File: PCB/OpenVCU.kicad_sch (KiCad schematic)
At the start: 25 parts, among them U1 STM32H743VIT6, Y1 ABM8-272-T3, Y2 CM315D32768DZFT

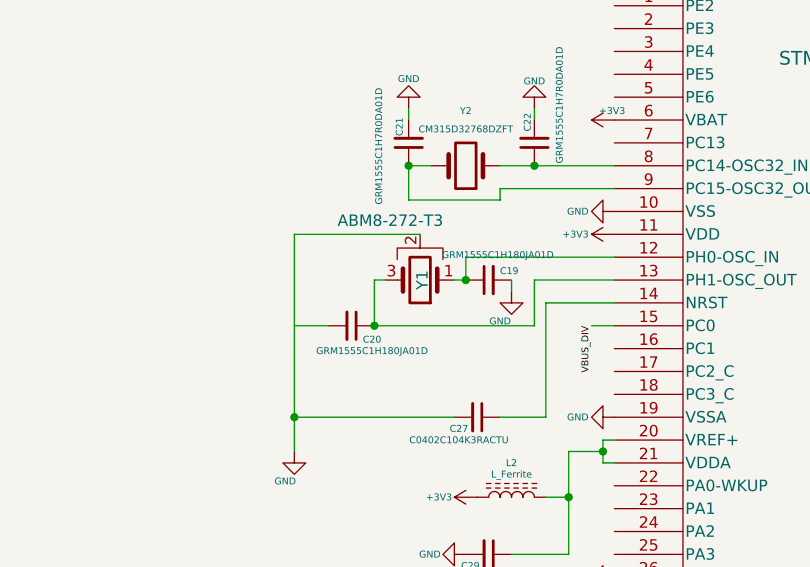
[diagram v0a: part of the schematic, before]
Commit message: Power sheet P2: USB-C fix, buck replacement, LDO rewire, battery sense, pull-downs
- Replaced MP1584 buck with TPS54360 (EOL fix)
- Fixed USB-C: CC pull-downs, ESD wiring, VBUS path, shell ground
- Rewired LDO: VIN<-+5V, GND->GND, VOUT->+3V3, caps at pins
- Added battery sense divider (100k/10k from VBAT)
- Added SBU1/SBU2 1M pull-downs (R38, R39)
- Fixed component rotations for distinct pin tips (90°)
- Added PWR_FLAGS on +5V rail (source) and VBUS net
- Added SBU1/SBU2 1M pull-downs (R38, R39)
- Removed old MP1584 debris
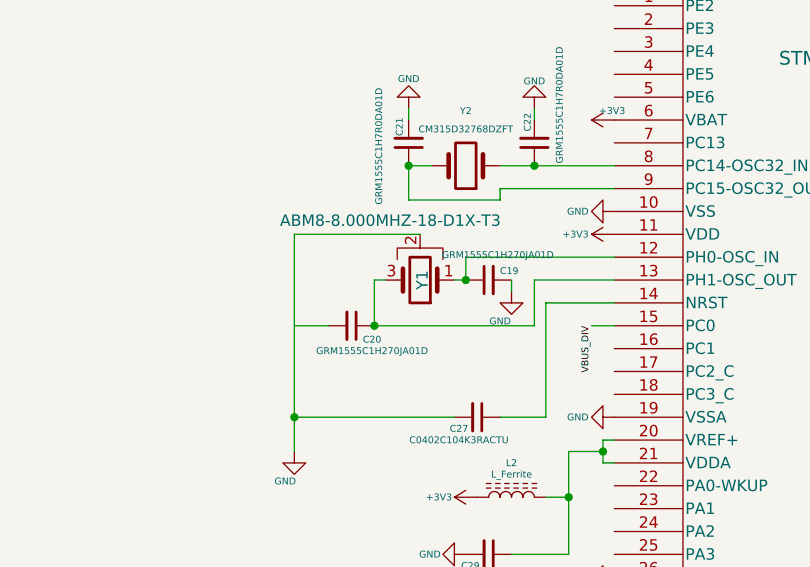
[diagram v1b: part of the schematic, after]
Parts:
- C19, C20: value GRM1555C1H180JA01D -> GRM1555C1H270JA01D; footprint GRM1555C1H180JA01D:CAPC1005X55N -> GRM1555C1H270JA01D:CAPC1005X55N; Check_prices https://www.snapeda.com/parts/GRM1555C1H180JA01D/Murata/vie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 -> https://www.snapeda.com/parts/GRM1555C1H270JA01D/Murata/vie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; MP GRM1555C1H180JA01D -> GRM1555C1H270JA01D; SnapEDA_Link https://www.snapeda.com/parts/GRM1555C1H180JA01D/Murata/vie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 -> https://www.snapeda.com/parts/GRM1555C1H270JA01D/Murata/vie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
- Y1: value ABM8-272-T3 -> ABM8-8.000MHZ-18-D1X-T3; footprint ABM8-272-T3:XTAL_ABM8-272-T3 -> ABM8-8.000MHZ-18-D1X-T3:XTAL_ABM8-8.000MHZ-18-D1X-T3; Check_prices https://www.snapeda.com/parts/ABM8-272-T3/Abracon/view-part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 -> https://www.snapeda.com/parts/ABM8-8.000MHZ-18-D1X-T3/Abrac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; MP ABM8-272-T3 -> ABM8-8.000MHZ-18-D1X-T3; Purchase-URL https://www.snapeda.com/api/url_track_click_mouser/?unipart_id=15805472&manufacturer=ABRACON&part_name=ABM8-272-T3&search_term=None -> https://www.snapeda.com/api/url_track_click_mouser/?unipart_id=15805472&manufacturer=ABRACON&part_name=ABM8-8.000MHZ-18-D1X-T3&search_term=None; SnapEDA_Link https://www.snapeda.com/parts/ABM8-272-T3/Abracon/view-part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 -> https://www.snapeda.com/parts/ABM8-8.000MHZ-18-D1X-T3/Abrac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

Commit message: Hierarchy: Power sheet hierarchical labels + root sheet pins (via Konnect)
- Added 5 hierarchical labels to Power.kicad_sch (VBAT, USB_D_P, USB_D_N, VBUS_SENSE, VBUS_DIV)
- Imported matching sheet pins onto root Power instance
- validate_sheet_pins: 0 issues; both files parse cleanly
- Root cause of A1: sub-sheets had only local labels, zero hierarchical labels
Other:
- sheet Power ports: added USB_D_N, USB_D_P, VBAT, VBUS_DIV, VBUS_SENSE; removed none
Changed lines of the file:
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@@
 			)
+		)
+		(pin "USB_D_P" bidirectional
+			(at 266.7 73.66 0)
+		)
+		(pin "USB_D_N" bidirectional
+			(at 266.7 76.2 0)
+		)
+		(pin "VBUS_SENSE" output
+			(at 266.7 78.74 0)
+		)
+		(pin "VBUS_DIV" output
+			(at 266.7 81.28 0)
+		)
+		(pin "VBAT" input
+			(at 266.7 83.82 0)
 		)
 		(instances

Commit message: Hierarchy: Sensors sheet hierarchical labels + root sheet pins (via Konnect)
- Added 8 hierarchical labels to Sensors.kicad_sch
- Fixed net-name mismatch: IMU_CS->SPI_CS_ACCEL, IMU_INT1->BMI_INT1 (match root MCU labels)
- Imported matching sheet pins on root Sensors instance
- validate_sheet_pins: 0 issues
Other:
- sheet Sensors ports: added BARO_INT, BMI_INT1, I2C1_SCL, I2C1_SDA, SPI1_MISO, SPI1_MOSI, SPI1_SCK, SPI_CS_ACCEL; removed none
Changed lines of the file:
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@@
 			)
+		)
+		(pin "SPI_CS_ACCEL" bidirectional
+			(at 266.7 38.1 0)
+		)
+		(pin "BMI_INT1" bidirectional
+			(at 266.7 40.64 0)
+		)
+		(pin "SPI1_SCK" bidirectional
+			(at 266.7 43.18 0)
+		)
+		(pin "SPI1_MOSI" bidirectional
+			(at 266.7 45.72 0)
+		)
+		(pin "SPI1_MISO" bidirectional
+			(at 266.7 48.26 0)
+		)
+		(pin "I2C1_SCL" bidirectional
+			(at 266.7 50.8 0)
+		)
+		(pin "I2C1_SDA" bidirectional
+			(at 266.7 53.34 0)
+		)
+		(pin "BARO_INT" output
+			(at 266.7 55.88 0)
 		)
 		(instances

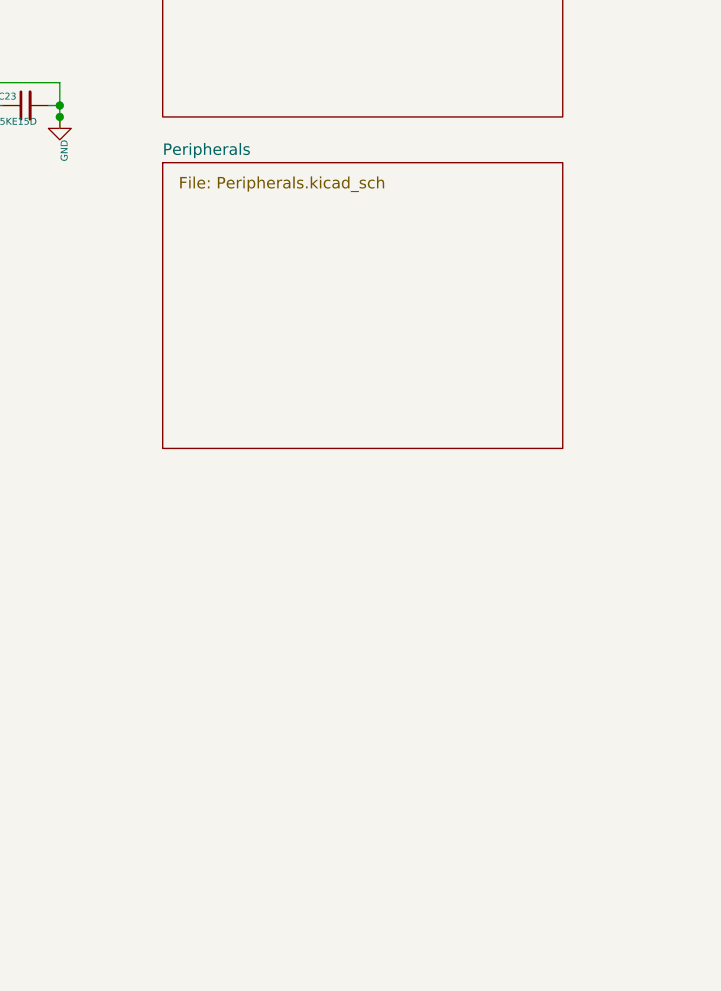
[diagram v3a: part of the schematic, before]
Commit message: Hierarchy: Peripherals sheet hierarchical labels + sheet pins (via Konnect)
- Added 27 hierarchical labels to Peripherals.kicad_sch
- Skipped dead leftover nets (L1_cap1, PWMx_R)
- Resized Peripherals sheet to 60x90mm to fit 27 pins on one edge
- Imported matching sheet pins on root Peripherals instance
- validate_sheet_pins: 0 issues across all three sheets
- Full hierarchy now valid: Power + Sensors + Peripherals all cross-linked
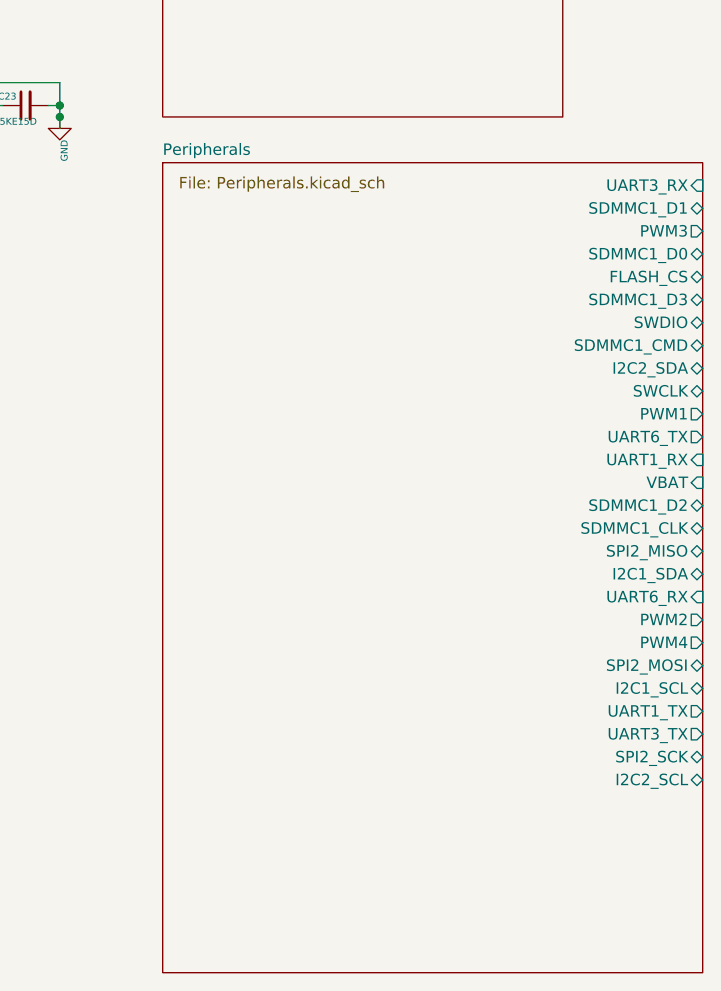
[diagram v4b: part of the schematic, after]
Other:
- sheet Peripherals ports: added FLASH_CS, I2C1_SCL, I2C1_SDA, I2C2_SCL, I2C2_SDA, PWM1, PWM2, PWM3, PWM4, SDMMC1_CLK, SDMMC1_CMD, SDMMC1_D0, SDMMC1_D1, SDMMC1_D2, SDMMC1_D3, SPI2_MISO, SPI2_MOSI, SPI2_SCK, SWCLK, SWDIO, UART1_RX, UART1_TX, UART3_RX, UART3_TX, UART6_RX, UART6_TX, VBAT; removed none
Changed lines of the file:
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@@
 	(sheet
 		(at 222.25 107.95)
-		(size 44.45 31.75)
+		(size 60 90)
 		(exclude_from_sim no)
 		(in_bom yes)
@@
 			)
 		)
+		(pin "UART3_RX" input
+			(at 282.25 110.49 0)
+		)
+		(pin "SDMMC1_D1" bidirectional
+			(at 282.25 113.03 0)
+		)
+		(pin "PWM3" output
+			(at 282.25 115.57 0)
+		)
+		(pin "SDMMC1_D0" bidirectional
+			(at 282.25 118.11 0)
+		)
+		(pin "FLASH_CS" bidirectional
+			(at 282.25 120.65 0)
+		)
+		(pin "SDMMC1_D3" bidirectional
+			(at 282.25 123.19 0)
+		)
+		(pin "SWDIO" bidirectional
+			(at 282.25 125.73 0)
+		)
+		(pin "SDMMC1_CMD" bidirectional
+			(at 282.25 128.27 0)
+		)
+		(pin "I2C2_SDA" bidirectional
+			(at 282.25 130.81 0)
+		)
+		(pin "SWCLK" bidirectional
+			(at 282.25 133.35 0)
+		)
+		(pin "PWM1" output
+			(at 282.25 135.89 0)
+		)
+		(pin "UART6_TX" output
+			(at 282.25 138.43 0)
+		)
+		(pin "UART1_RX" input
+			(at 282.25 140.97 0)
+		)
+		(pin "VBAT" input
+			(at 282.25 143.51 0)
+		)
+		(pin "SDMMC1_D2" bidirectional
+			(at 282.25 146.05 0)
+		)
+		(pin "SDMMC1_CLK" bidirectional
+			(at 282.25 148.59 0)
+		)
+		(pin "SPI2_MISO" bidirectional
+			(at 282.25 151.13 0)
+		)
+		(pin "I2C1_SDA" bidirectional
+			(at 282.25 153.67 0)
+		)
+		(pin "UART6_RX" input
+			(at 282.25 156.21 0)
+		)
+		(pin "PWM2" output
+			(at 282.25 158.75 0)
+		)
+		(pin "PWM4" output
+			(at 282.25 161.29 0)
+		)
+		(pin "SPI2_MOSI" bidirectional
+			(at 282.25 163.83 0)
+		)
+		(pin "I2C1_SCL" bidirectional
+			(at 282.25 166.37 0)
+		)
+		(pin "UART1_TX" output
+			(at 282.25 168.91 0)
+		)
+		(pin "UART3_TX" output
+			(at 282.25 171.45 0)
+		)
+		(pin "SPI2_SCK" bidirectional
+			(at 282.25 173.99 0)
+		)
+		(pin "I2C2_SCL" bidirectional
+			(at 282.25 176.53 0)
+		)
 		(instances
